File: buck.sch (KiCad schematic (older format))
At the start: 23 parts, among them U3 MD7133H, U5 MP1584EN, U6 INA199A1DCKR

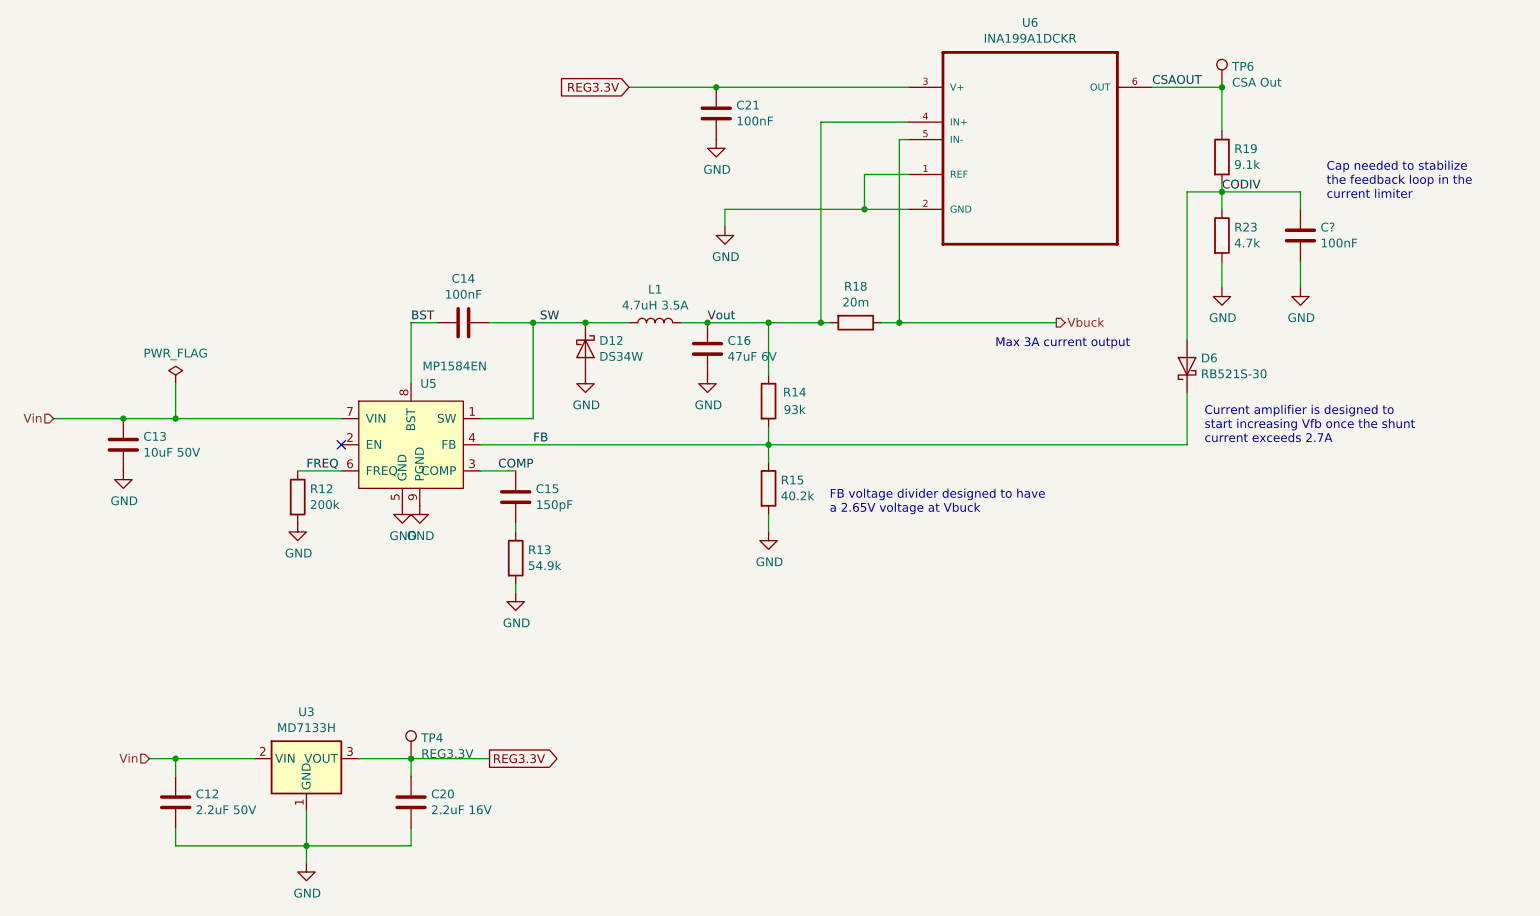
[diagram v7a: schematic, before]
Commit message: Prevent reverse current through regulator
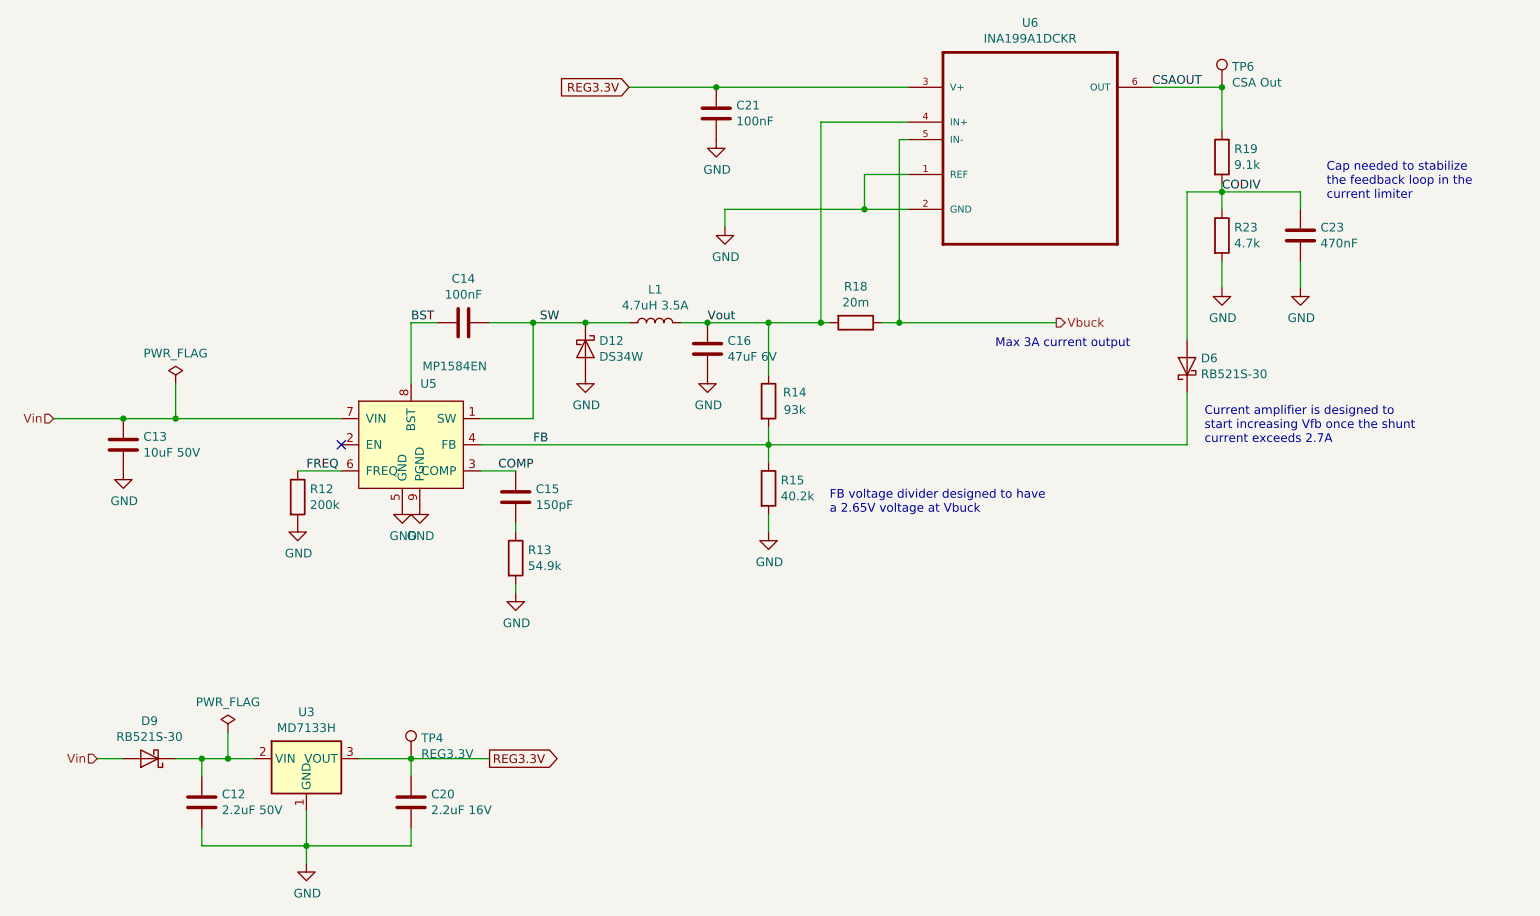
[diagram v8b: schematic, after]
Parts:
- added D9: RB521S-30, Diode_SMD:D_SOD-523, symbol Device:D_Schottky
- C23: renamed from C?; value 100nF -> 470nF
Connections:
- net Vin: now also D9.2 (A); no longer C12.1, U3.2 (VIN)
- new net: C12.1, D9.1 (K), U3.2 (VIN)
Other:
- moved on the sheet: C12
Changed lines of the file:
@@
 L Device:C C12
 U 1 1 5E278894
-P 1600 5400
-F 0 "C12" H 1715 5446 50  0000 L CNN
-F 1 "2.2uF 50V" H 1715 5355 50  0000 L CNN
-F 2 "Capacitor_SMD:C_1206_3216Metric" H 1638 5250 50  0001 C CNN
-F 3 "~" H 1600 5400 50  0001 C CNN
-	1    1600 5400
+P 1750 5400
+F 0 "C12" H 1865 5446 50  0000 L CNN
+F 1 "2.2uF 50V" H 1865 5355 50  0000 L CNN
+F 2 "Capacitor_SMD:C_1206_3216Metric" H 1788 5250 50  0001 C CNN
+F 3 "~" H 1750 5400 50  0001 C CNN
+	1    1750 5400
 	1    0    0    -1
 $EndComp
@@
 $EndComp
 Wire Wire Line
-	1600 5250 1600 5150
-Wire Wire Line
-	1600 5150 2050 5150
-Wire Wire Line
 	2650 5150 2950 5150
 Wire Wire Line
 	2950 5150 2950 5250
-Wire Wire Line
-	1600 5550 1600 5650
-Wire Wire Line
-	1600 5650 2350 5650
 Wire Wire Line
 	2950 5650 2950 5550
@@
 	1    0    0    -1
 $EndComp
-Text HLabel 1450 5150 0    50   Input ~ 0
+Text HLabel 1150 5150 0    50   Input ~ 0
 Vin
 Wire Wire Line
@@
 Text GLabel 4200 1300 0    50   Input ~ 0
 REG3.3V
-Wire Wire Line
-	1450 5150 1600 5150
-Connection ~ 1600 5150
 Text GLabel 3400 5150 2    50   Output ~ 0
 REG3.3V
@@
 NoConn ~ 2550 3350
 $Comp
-L Device:C C?
+L Device:C C23
 U 1 1 5E563B66
 P 8050 2150
-F 0 "C?" H 8165 2196 50  0000 L CNN
-F 1 "100nF" H 8165 2105 50  0000 L CNN
+F 0 "C23" H 8165 2196 50  0000 L CNN
+F 1 "470nF" H 8165 2105 50  0000 L CNN
 F 2 "Capacitor_SMD:C_0603_1608Metric_Pad1.05x0.95mm_HandSolder" H 8088 2000 50  0001 C CNN
 F 3 "~" H 8050 2150 50  0001 C CNN
@@
 AR Path="/5E566874" Ref="#PWR?"  Part="1"
 AR Path="/5C3476D8/5E566874" Ref="#PWR?"  Part="1"
-AR Path="/5CA65CC5/5E566874" Ref="#PWR?"  Part="1"
-F 0 "#PWR?" H 8050 2200 50  0001 C CNN
+AR Path="/5CA65CC5/5E566874" Ref="#PWR0109"  Part="1"
+F 0 "#PWR0109" H 8050 2200 50  0001 C CNN
 F 1 "GND" H 8055 2277 50  0000 C CNN
 F 2 "" H 8050 2450 50  0001 C CNN
@@
 Text Notes 8200 1950 0    50   ~ 0
 Cap needed to stabilize\nthe feedback loop in the \ncurrent limiter
+Wire Wire Line
+	1150 5150 1300 5150
+Wire Wire Line
+	1750 5250 1750 5150
+Connection ~ 1750 5150
+Wire Wire Line
+	1750 5150 1900 5150
+Wire Wire Line
+	1750 5550 1750 5650
+Wire Wire Line
+	1750 5650 2350 5650
+$Comp
+L Device:D_Schottky D9
+U 1 1 5E5A1A2A
+P 1450 5150
+F 0 "D9" H 1450 4934 50  0000 C CNN
+F 1 "RB521S-30" H 1450 5025 50  0000 C CNN
+F 2 "Diode_SMD:D_SOD-523" H 1450 5150 50  0001 C CNN
+F 3 "~" H 1450 5150 50  0001 C CNN
+	1    1450 5150
+	-1   0    0    1
+$EndComp
+Wire Wire Line
+	1600 5150 1750 5150
+$Comp
+L power:PWR_FLAG #FLG?
+U 1 1 5E5BA0FA
+P 1900 5000
+AR Path="/5C3476D8/5E5BA0FA" Ref="#FLG?"  Part="1"
+AR Path="/5CA65CC5/5E5BA0FA" Ref="#FLG0105"  Part="1"
+F 0 "#FLG0105" H 1900 5075 50  0001 C CNN
+F 1 "PWR_FLAG" H 1900 5174 50  0000 C CNN
+F 2 "" H 1900 5000 50  0001 C CNN
+F 3 "~" H 1900 5000 50  0001 C CNN
+	1    1900 5000
+	1    0    0    -1
+$EndComp
+Wire Wire Line
+	1900 5000 1900 5150
+Connection ~ 1900 5150
+Wire Wire Line
+	1900 5150 2050 5150
 $EndSCHEMATC
